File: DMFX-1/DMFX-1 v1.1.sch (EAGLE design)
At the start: 567 parts, among them IC2 SN74HC4066D, J1 USB-MINIB-5PIN, J1-2 USB-MINIB-5PIN, J10 MONOSW3C, J11 DM3BT-DSF-PEJS, J2 USB-B-SMT, J3 STEREOSW3C, J4 HEADPHONES, J5 87409-110LF, J6 DM3BT-DSF-PEJS, J7 87409-110LF, J8 DCJ0202, J9 MONOSW3C, Q1 MUN2214T1, Q10 MUN2214T1, Q2 MUN2214T1, Q3 MMBF4393, Q4 MUN2214T1, Q5 2N7002ET1G, Q6 2N7002ET1G, Q7 2N7002ET1G, Q8 MUN2214T1, Q9 MUN2214T1, SW1 MB2011SB1W03-DA, SW2 OS102011MA1Q, U10X 24C64SM, U11X TPS73201DBVT, U12X TPS562209SO, U13 741G3157DBVR, U14 ASDM1-12.000MHZ-LC-T, U15X CDCLVC1108PWR, U17 TLV320AIC3204IRHBT, U18 SN74CBTLV3245APW, U19 LME49721, U1X TPS562209SO, U2 AT93C46A-10TQ-2.7, U20 LME49721, U21 LME49721, U22 LME49721, U23 LME49721, U24 LMV358, U3X TPS3803-01DCKR, U4 TMS320C5535, U5 TMS320C5535, U6 FT2232HL, U7 TPD2E001IDRLRQ1, U8 74LVC1G175DBVSOT95, U9 W25Q64FVSFIG, U9-2 W25Q64FVSFIG, Y1 32.768kHz, Y1-2 32.768kHz

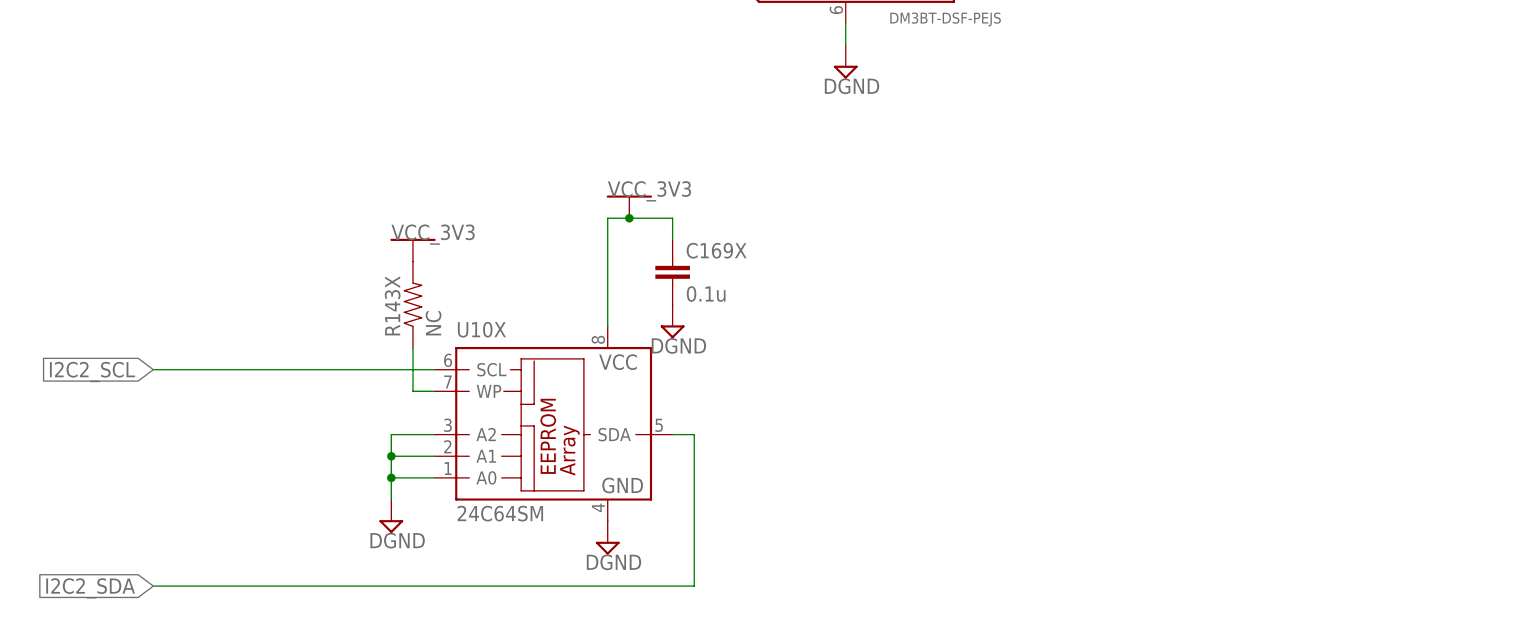
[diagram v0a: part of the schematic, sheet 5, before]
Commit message: 
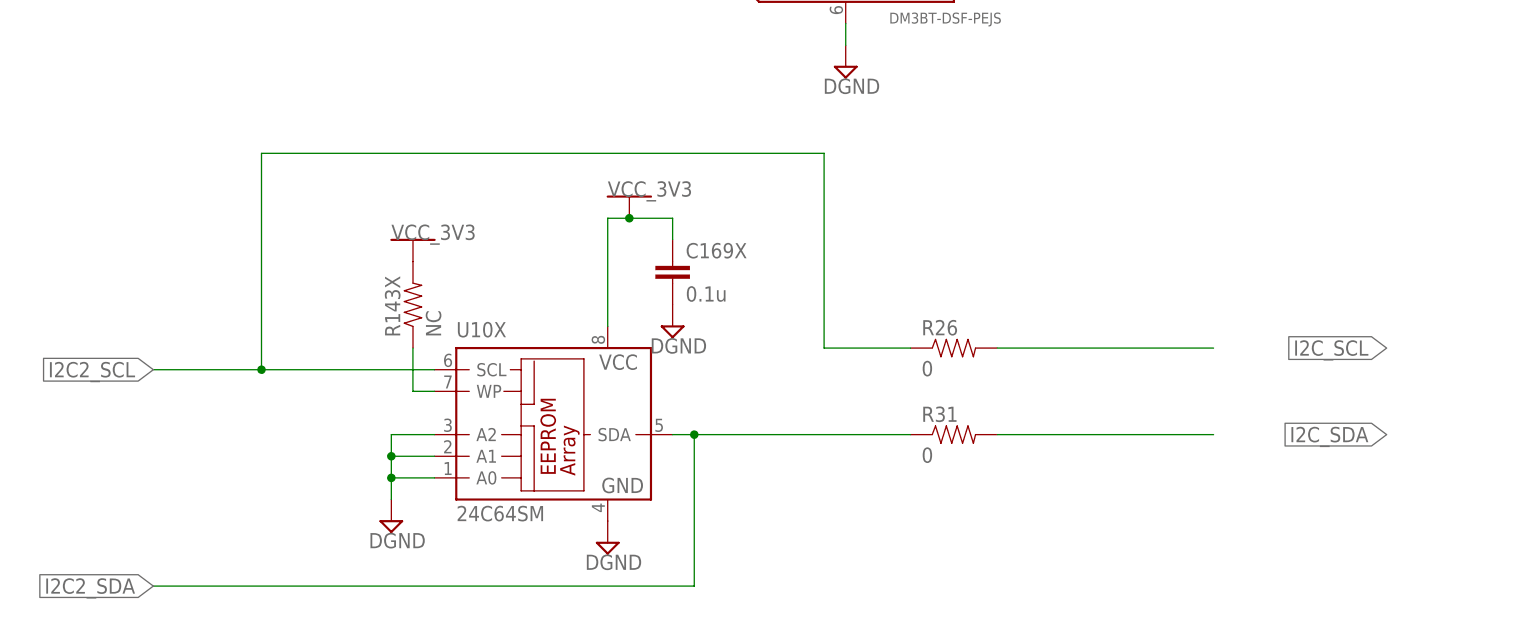
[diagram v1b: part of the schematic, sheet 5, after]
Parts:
- added R26, R31: 0, SparkFun:RESISTOR0402-RES
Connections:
- net I2C2_SCL: now also R26.1
- net I2C2_SDA: now also R31.1
- net I2C_SCL: now also R26.2
- net I2C_SDA: now also R31.2
- net N$138: now also U22A.-IN; no longer U22A.+IN
- net N$149: now also U23A.-IN; no longer U23A.+IN
- net V1.65: now also U22A.+IN, U23A.+IN; no longer U22A.-IN, U23A.-IN
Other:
- moved on the sheet: U22A, U23A
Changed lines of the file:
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@@
 <part name="R24" library="SparkFun" deviceset="RESISTOR" device="0402-RES" value="NC"/>
 <part name="U$120" library="rezzonics" deviceset="VCC_3V3" device=""/>
+<part name="R26" library="SparkFun" deviceset="RESISTOR" device="0402-RES" value="0">
+<attribute name="MPN" value="ERJ-2GE0R00X"/>
+</part>
+<part name="R31" library="SparkFun" deviceset="RESISTOR" device="0402-RES" value="0">
+<attribute name="MPN" value="ERJ-2GE0R00X"/>
+</part>
 </parts>
 <sheets>
@@
 </instance>
 <instance part="U$171" gate="G$1" x="294.64" y="190.5"/>
+<instance part="R26" gate="G$1" x="147.32" y="50.8">
+<attribute name="MPN" x="147.32" y="50.8" size="1.778" layer="96" display="off"/>
+</instance>
+<instance part="R31" gate="G$1" x="147.32" y="40.64">
+<attribute name="MPN" x="147.32" y="40.64" size="1.778" layer="96" display="off"/>
+</instance>
 </instances>
 <busses>
@@
 <segment>
 <pinref part="U10X" gate="G$1" pin="SCL"/>
-<wire x1="86.36" y1="48.26" x2="53.34" y2="48.26" width="0.1524" layer="91"/>
+<wire x1="86.36" y1="48.26" x2="66.04" y2="48.26" width="0.1524" layer="91"/>
 <label x="53.34" y="48.26" size="1.778" layer="95" rot="R180" xref="yes"/>
+<wire x1="66.04" y1="48.26" x2="53.34" y2="48.26" width="0.1524" layer="91"/>
+<wire x1="66.04" y1="48.26" x2="66.04" y2="73.66" width="0.1524" layer="91"/>
+<wire x1="66.04" y1="73.66" x2="132.08" y2="73.66" width="0.1524" layer="91"/>
+<wire x1="132.08" y1="73.66" x2="132.08" y2="50.8" width="0.1524" layer="91"/>
+<pinref part="R26" gate="G$1" pin="1"/>
+<wire x1="132.08" y1="50.8" x2="142.24" y2="50.8" width="0.1524" layer="91"/>
+<junction x="66.04" y="48.26"/>
 </segment>
 </net>
@@
 <wire x1="116.84" y1="40.64" x2="114.3" y2="40.64" width="0.1524" layer="91"/>
 <label x="53.34" y="22.86" size="1.778" layer="95" rot="R180" xref="yes"/>
+<pinref part="R31" gate="G$1" pin="1"/>
+<wire x1="116.84" y1="40.64" x2="142.24" y2="40.64" width="0.1524" layer="91"/>
+<junction x="116.84" y="40.64"/>
 </segment>
 </net>
@@
 </segment>
 </net>
+<net name="I2C_SCL" class="0">
+<segment>
+<pinref part="R26" gate="G$1" pin="2"/>
+<wire x1="152.4" y1="50.8" x2="177.8" y2="50.8" width="0.1524" layer="91"/>
+<label x="198.12" y="50.8" size="1.778" layer="95" rot="R180" xref="yes"/>
+</segment>
+</net>
+<net name="I2C_SDA" class="0">
+<segment>
+<pinref part="R31" gate="G$1" pin="2"/>
+<wire x1="152.4" y1="40.64" x2="177.8" y2="40.64" width="0.1524" layer="91"/>
+<label x="198.12" y="40.64" size="1.778" layer="95" rot="R180" xref="yes"/>
+</segment>
+</net>
 </nets>
 </sheet>
@@
 </segment>
 <segment>
-<wire x1="88.9" y1="48.26" x2="88.9" y2="43.18" width="0.1524" layer="91"/>
 <pinref part="R222X" gate="G$1" pin="1"/>
 <wire x1="88.9" y1="43.18" x2="101.6" y2="43.18" width="0.1524" layer="91"/>
@@
 <attribute name="MPN" x="101.6" y="243.84" size="1.778" layer="96" display="off"/>
 </instance>
-<instance part="U22" gate="A" x="132.08" y="215.9"/>
+<instance part="U22" gate="A" x="132.08" y="215.9" rot="MR180"/>
 <instance part="U22" gate="P" x="132.08" y="215.9"/>
 <instance part="C190" gate="G$1" x="175.26" y="223.52" rot="R90">
@@
 <attribute name="MPN" x="101.6" y="162.56" size="1.778" layer="96" display="off"/>
 </instance>
-<instance part="U23" gate="A" x="132.08" y="134.62"/>
+<instance part="U23" gate="A" x="132.08" y="134.62" rot="MR180"/>
 <instance part="U23" gate="P" x="132.08" y="134.62"/>
 <instance part="C200" gate="G$1" x="175.26" y="142.24" rot="R90">
@@
 <pinref part="C189" gate="G$1" pin="1"/>
 <wire x1="121.92" y1="233.68" x2="127" y2="233.68" width="0.1524" layer="91"/>
-<pinref part="U22" gate="A" pin="+IN"/>
+<pinref part="U22" gate="A" pin="-IN"/>
 <wire x1="121.92" y1="218.44" x2="124.46" y2="218.44" width="0.1524" layer="91"/>
 <junction x="121.92" y="218.44"/>
@@
 <pinref part="C197" gate="G$1" pin="1"/>
 <wire x1="121.92" y1="152.4" x2="127" y2="152.4" width="0.1524" layer="91"/>
-<pinref part="U23" gate="A" pin="+IN"/>
+<pinref part="U23" gate="A" pin="-IN"/>
 <wire x1="121.92" y1="137.16" x2="124.46" y2="137.16" width="0.1524" layer="91"/>
 <junction x="121.92" y="137.16"/>
@@
 <wire x1="116.84" y1="205.74" x2="116.84" y2="203.2" width="0.1524" layer="91"/>
 <wire x1="121.92" y1="213.36" x2="121.92" y2="203.2" width="0.1524" layer="91"/>
-<pinref part="U22" gate="A" pin="-IN"/>
-<wire x1="121.92" y1="213.36" x2="124.46" y2="213.36" width="0.1524" layer="91"/>
 <wire x1="116.84" y1="203.2" x2="121.92" y2="203.2" width="0.1524" layer="91"/>
 <pinref part="U$164" gate="G$1" pin="V1.65"/>
+<pinref part="U22" gate="A" pin="+IN"/>
+<wire x1="124.46" y1="213.36" x2="121.92" y2="213.36" width="0.1524" layer="91"/>
 </segment>
 <segment>
@@
 <wire x1="116.84" y1="124.46" x2="116.84" y2="121.92" width="0.1524" layer="91"/>
 <wire x1="121.92" y1="132.08" x2="121.92" y2="121.92" width="0.1524" layer="91"/>
-<pinref part="U23" gate="A" pin="-IN"/>
-<wire x1="121.92" y1="132.08" x2="124.46" y2="132.08" width="0.1524" layer="91"/>
 <wire x1="116.84" y1="121.92" x2="121.92" y2="121.92" width="0.1524" layer="91"/>
 <pinref part="U$166" gate="G$1" pin="V1.65"/>
+<pinref part="U23" gate="A" pin="+IN"/>
+<wire x1="124.46" y1="132.08" x2="121.92" y2="132.08" width="0.1524" layer="91"/>
 </segment>
 <segment>
